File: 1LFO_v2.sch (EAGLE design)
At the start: 23 parts, among them IC1 LM324D

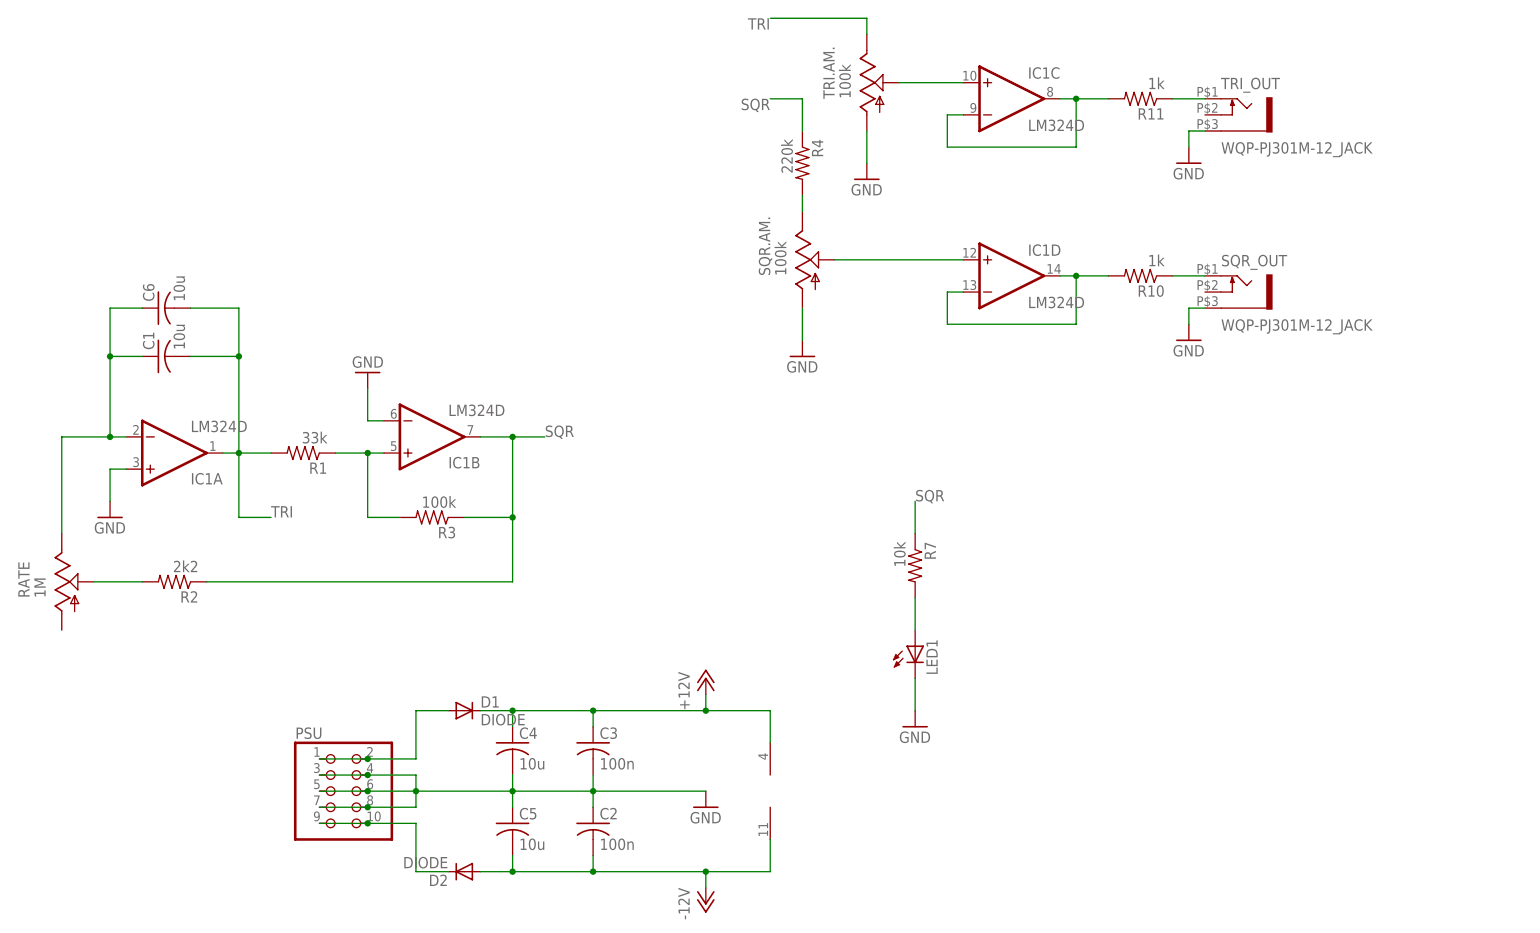
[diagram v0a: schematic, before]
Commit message: Added switch to select LFO rate range. Moved IC1 & rerouted to make room for the same.
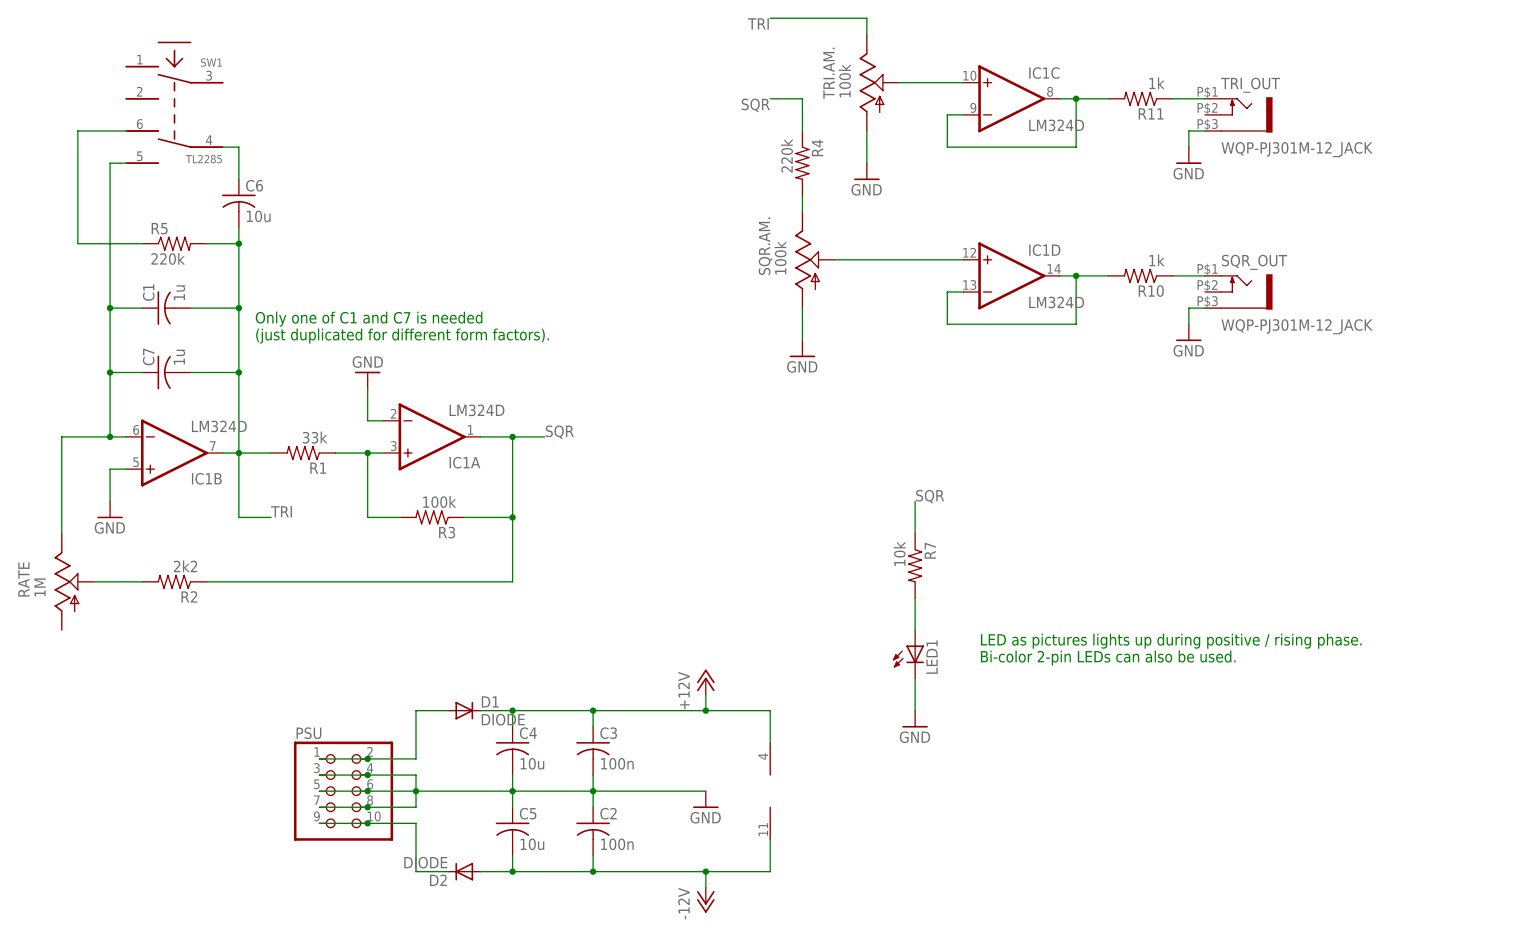
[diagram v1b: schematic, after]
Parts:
- added C7: 1u, rcl:C-USC0603K
- added R5: 220k, rcl:R-US_R0603
- added SW1: TL2285, lb_devs:TL2285
- C1: value 10u -> 1u
- C6: device rcl:C-USC0603K -> rcl:C-USC1206K
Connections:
- new net N$4: C6.1, SW1.P4
- new net N$6: R5.1, SW1.P6
- net GND: now also IC1A.-IN, IC1B.+IN; no longer IC1A.+IN, IC1B.-IN
- net N$1: now also C7.1, IC1B.-IN, SW1.P5; no longer C6.1, IC1A.-IN
- net N$5: now also IC1A.+IN; no longer IC1B.+IN
- net SQR: now also IC1A.OUT; no longer IC1B.OUT
- net TRI: now also C7.2, IC1B.OUT, R5.2; no longer IC1A.OUT
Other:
- note added: "LED as pictures lights up during positive / rising phase. Bi-color 2-pin LEDs can also be used."
- note added: "Only one of C1 and C7 is needed (just duplicated for different form factors)."
- moved on the sheet: C1, C6, IC1A, IC1B
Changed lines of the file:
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@@
 <part name="FRAME1" library="frames" deviceset="A4L-LOC" device=""/>
 <part name="IC1" library="linear" deviceset="LM324" device="D"/>
-<part name="C1" library="rcl" deviceset="C-US" device="C1206K" value="10u"/>
+<part name="C1" library="rcl" deviceset="C-US" device="C1206K" value="1u"/>
 <part name="C2" library="rcl" deviceset="C-US" device="C0603K" value="100n"/>
 <part name="C3" library="rcl" deviceset="C-US" device="C0603K" value="100n"/>
@@
 <part name="P+1" library="supply1" deviceset="+12V" device=""/>
 <part name="P-1" library="supply1" deviceset="-12V" device=""/>
-<part name="C6" library="rcl" deviceset="C-US" device="C0603K" value="10u"/>
+<part name="C6" library="rcl" deviceset="C-US" device="C1206K" value="10u"/>
 <part name="R10" library="rcl" deviceset="R-US_" device="R0603" value="1k"/>
 <part name="R11" library="rcl" deviceset="R-US_" device="R0603" value="1k"/>
@@
 <part name="GND9" library="supply1" deviceset="GND" device=""/>
 <part name="R4" library="rcl" deviceset="R-US_" device="R0603" value="220k"/>
+<part name="SW1" library="lb_devs" deviceset="TL2285" device=""/>
+<part name="R5" library="rcl" deviceset="R-US_" device="R0603" value="220k"/>
+<part name="C7" library="rcl" deviceset="C-US" device="C0603K" value="1u"/>
 </parts>
 <sheets>
 <sheet>
 <plain>
+<text x="58.42" y="101.6" size="1.778" layer="91">Only one of C1 and C7 is needed
+(just duplicated for different form factors).</text>
+<text x="172.72" y="50.8" size="1.778" layer="91">LED as pictures lights up during positive / rising phase.
+Bi-color 2-pin LEDs can also be used.</text>
 </plain>
 <instances>
 <instance part="FRAME1" gate="G$1" x="0" y="0"/>
-<instance part="IC1" gate="A" x="45.72" y="83.82" rot="MR180"/>
-<instance part="IC1" gate="B" x="86.36" y="86.36" rot="MR180"/>
+<instance part="IC1" gate="B" x="45.72" y="83.82" rot="MR180"/>
+<instance part="IC1" gate="A" x="86.36" y="86.36" rot="MR180"/>
 <instance part="IC1" gate="C" x="177.8" y="139.7"/>
 <instance part="IC1" gate="D" x="177.8" y="111.76"/>
-<instance part="C1" gate="G$1" x="43.18" y="99.06" rot="R90"/>
+<instance part="C1" gate="G$1" x="43.18" y="106.68" rot="R90"/>
 <instance part="C2" gate="G$1" x="111.76" y="25.4"/>
 <instance part="C3" gate="G$1" x="111.76" y="38.1"/>
@@
 <instance part="P+1" gate="1" x="129.54" y="48.26"/>
 <instance part="P-1" gate="1" x="129.54" y="12.7"/>
-<instance part="C6" gate="G$1" x="43.18" y="106.68" rot="R90"/>
+<instance part="C6" gate="G$1" x="55.88" y="124.46"/>
 <instance part="R10" gate="G$1" x="198.12" y="111.76" rot="R180"/>
 <instance part="R11" gate="G$1" x="198.12" y="139.7" rot="R180"/>
@@
 <instance part="GND9" gate="1" x="162.56" y="40.64"/>
 <instance part="R4" gate="G$1" x="144.78" y="129.54" rot="R270"/>
+<instance part="SW1" gate="G$1" x="45.72" y="137.16" rot="MR0"/>
+<instance part="R5" gate="G$1" x="45.72" y="116.84"/>
+<instance part="C7" gate="G$1" x="43.18" y="96.52" rot="R90"/>
 </instances>
 <busses>
@@
 <net name="N$1" class="0">
 <segment>
-<pinref part="IC1" gate="A" pin="-IN"/>
+<pinref part="IC1" gate="B" pin="-IN"/>
 <wire x1="38.1" y1="86.36" x2="35.56" y2="86.36" width="0.1524" layer="91"/>
 <pinref part="RATE" gate="G$1" pin="E"/>
 <wire x1="35.56" y1="86.36" x2="27.94" y2="86.36" width="0.1524" layer="91"/>
 <wire x1="27.94" y1="86.36" x2="27.94" y2="71.12" width="0.1524" layer="91"/>
-<wire x1="35.56" y1="86.36" x2="35.56" y2="99.06" width="0.1524" layer="91"/>
+<wire x1="35.56" y1="86.36" x2="35.56" y2="96.52" width="0.1524" layer="91"/>
 <pinref part="C1" gate="G$1" pin="1"/>
-<wire x1="35.56" y1="99.06" x2="40.64" y2="99.06" width="0.1524" layer="91"/>
+<wire x1="35.56" y1="96.52" x2="35.56" y2="106.68" width="0.1524" layer="91"/>
+<wire x1="35.56" y1="106.68" x2="40.64" y2="106.68" width="0.1524" layer="91"/>
 <junction x="35.56" y="86.36"/>
-<wire x1="35.56" y1="99.06" x2="35.56" y2="106.68" width="0.1524" layer="91"/>
-<pinref part="C6" gate="G$1" pin="1"/>
-<wire x1="35.56" y1="106.68" x2="40.64" y2="106.68" width="0.1524" layer="91"/>
-<junction x="35.56" y="99.06"/>
+<junction x="35.56" y="106.68"/>
+<wire x1="35.56" y1="106.68" x2="35.56" y2="129.54" width="0.1524" layer="91"/>
+<pinref part="SW1" gate="G$1" pin="P5"/>
+<wire x1="38.1" y1="129.54" x2="35.56" y2="129.54" width="0.1524" layer="91"/>
+<pinref part="C7" gate="G$1" pin="1"/>
+<wire x1="40.64" y1="96.52" x2="35.56" y2="96.52" width="0.1524" layer="91"/>
+<junction x="35.56" y="96.52"/>
 </segment>
 </net>
 <net name="TRI" class="0">
 <segment>
-<pinref part="IC1" gate="A" pin="OUT"/>
+<pinref part="IC1" gate="B" pin="OUT"/>
 <pinref part="R1" gate="G$1" pin="2"/>
 <wire x1="53.34" y1="83.82" x2="55.88" y2="83.82" width="0.1524" layer="91"/>
 <wire x1="55.88" y1="83.82" x2="60.96" y2="83.82" width="0.1524" layer="91"/>
-<wire x1="55.88" y1="83.82" x2="55.88" y2="99.06" width="0.1524" layer="91"/>
+<wire x1="55.88" y1="83.82" x2="55.88" y2="96.52" width="0.1524" layer="91"/>
 <pinref part="C1" gate="G$1" pin="2"/>
-<wire x1="55.88" y1="99.06" x2="48.26" y2="99.06" width="0.1524" layer="91"/>
+<wire x1="55.88" y1="96.52" x2="55.88" y2="106.68" width="0.1524" layer="91"/>
+<wire x1="55.88" y1="106.68" x2="48.26" y2="106.68" width="0.1524" layer="91"/>
 <junction x="55.88" y="83.82"/>
-<pinref part="C6" gate="G$1" pin="2"/>
-<wire x1="48.26" y1="106.68" x2="55.88" y2="106.68" width="0.1524" layer="91"/>
-<wire x1="55.88" y1="106.68" x2="55.88" y2="99.06" width="0.1524" layer="91"/>
-<junction x="55.88" y="99.06"/>
+<wire x1="55.88" y1="119.38" x2="55.88" y2="116.84" width="0.1524" layer="91"/>
+<junction x="55.88" y="106.68"/>
+<wire x1="55.88" y1="116.84" x2="55.88" y2="106.68" width="0.1524" layer="91"/>
 <wire x1="55.88" y1="83.82" x2="55.88" y2="73.66" width="0.1524" layer="91"/>
 <wire x1="55.88" y1="73.66" x2="60.96" y2="73.66" width="0.1524" layer="91"/>
 <label x="60.96" y="73.66" size="1.778" layer="95"/>
+<pinref part="C6" gate="G$1" pin="2"/>
+<pinref part="R5" gate="G$1" pin="2"/>
+<wire x1="50.8" y1="116.84" x2="55.88" y2="116.84" width="0.1524" layer="91"/>
+<junction x="55.88" y="116.84"/>
+<pinref part="C7" gate="G$1" pin="2"/>
+<wire x1="48.26" y1="96.52" x2="55.88" y2="96.52" width="0.1524" layer="91"/>
+<junction x="55.88" y="96.52"/>
 </segment>
 <segment>
@@
 <segment>
 <pinref part="R1" gate="G$1" pin="1"/>
-<pinref part="IC1" gate="B" pin="+IN"/>
+<pinref part="IC1" gate="A" pin="+IN"/>
 <wire x1="71.12" y1="83.82" x2="76.2" y2="83.82" width="0.1524" layer="91"/>
 <wire x1="76.2" y1="83.82" x2="78.74" y2="83.82" width="0.1524" layer="91"/>
@@
 <net name="SQR" class="0">
 <segment>
-<pinref part="IC1" gate="B" pin="OUT"/>
+<pinref part="IC1" gate="A" pin="OUT"/>
 <wire x1="93.98" y1="86.36" x2="99.06" y2="86.36" width="0.1524" layer="91"/>
 <wire x1="99.06" y1="86.36" x2="99.06" y2="73.66" width="0.1524" layer="91"/>
@@
 <net name="GND" class="0">
 <segment>
-<pinref part="IC1" gate="A" pin="+IN"/>
+<pinref part="IC1" gate="B" pin="+IN"/>
 <wire x1="38.1" y1="81.28" x2="35.56" y2="81.28" width="0.1524" layer="91"/>
 <wire x1="35.56" y1="81.28" x2="35.56" y2="76.2" width="0.1524" layer="91"/>
@@
 </segment>
 <segment>
-<pinref part="IC1" gate="B" pin="-IN"/>
+<pinref part="IC1" gate="A" pin="-IN"/>
 <wire x1="78.74" y1="88.9" x2="76.2" y2="88.9" width="0.1524" layer="91"/>
 <wire x1="76.2" y1="88.9" x2="76.2" y2="93.98" width="0.1524" layer="91"/>
@@
 </segment>
 </net>
+<net name="N$4" class="0">
+<segment>
+<pinref part="SW1" gate="G$1" pin="P4"/>
+<pinref part="C6" gate="G$1" pin="1"/>
+<wire x1="53.34" y1="132.08" x2="55.88" y2="132.08" width="0.1524" layer="91"/>
+<wire x1="55.88" y1="132.08" x2="55.88" y2="127" width="0.1524" layer="91"/>
+</segment>
+</net>
+<net name="N$6" class="0">
+<segment>
+<pinref part="R5" gate="G$1" pin="1"/>
+<wire x1="40.64" y1="116.84" x2="30.48" y2="116.84" width="0.1524" layer="91"/>
+<wire x1="30.48" y1="116.84" x2="30.48" y2="134.62" width="0.1524" layer="91"/>
+<pinref part="SW1" gate="G$1" pin="P6"/>
+<wire x1="30.48" y1="134.62" x2="38.1" y2="134.62" width="0.1524" layer="91"/>
+</segment>
+</net>
 </nets>
 </sheet>
@@
 </schematic>
 </drawing>
+<compatibility>
+<note version="6.3" minversion="6.2.2" severity="warning">
+Since Version 6.2.2 text objects can contain more than one line,
+which will not be processed correctly with this version.
+</note>
+</compatibility>
 </eagle>
